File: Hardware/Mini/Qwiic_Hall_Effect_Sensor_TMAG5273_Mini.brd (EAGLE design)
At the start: 25.4 x 12.7 mm, 40 parts, among them J1 Vertical Qwiic Connector, J2 Vertical Qwiic Connector, Q1 20V/4.2A/52mΩ/1.4W, U1 TMAG5273

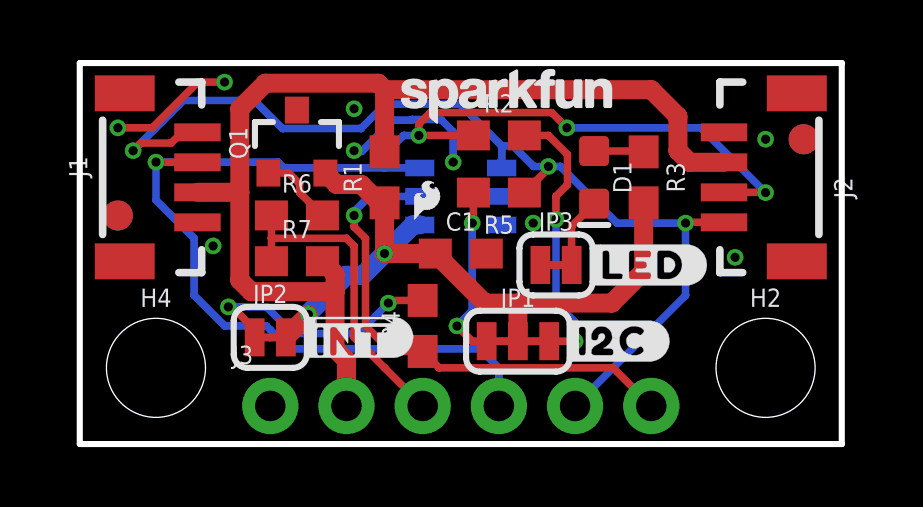
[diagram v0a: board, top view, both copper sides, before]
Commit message: Updates for design review
Changed LED and associated resistor to have the correct part and value; added dimension lines and further notes on the layout; adjusted aesthetics in schematic to now be the same as each other (minus the change in Qwiic connectors and number of standoffs)
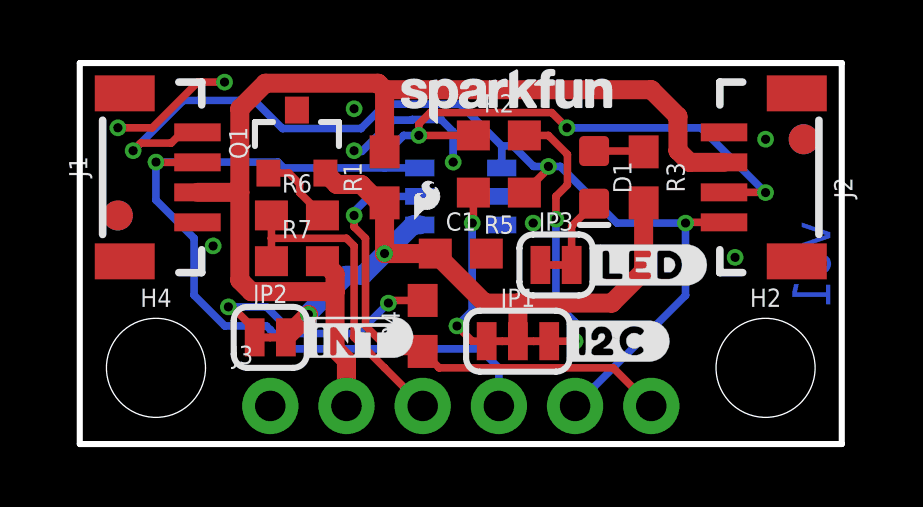
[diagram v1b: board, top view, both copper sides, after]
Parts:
- D1: value RED -> Red
- R3: value 1k -> 4.7k
- moved LOGO5 48.3 mm to (44.5, 50.8)
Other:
- board text added: "Solder Mask: Red Thickness: 1.6mm Two layer design Finish: HASL Lead-Free Copper Weight: 1oz Material: TG135-140"
- board text added: "v01"
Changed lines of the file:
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@@
 <layer number="45" name="Holes" color="7" fill="1" visible="yes" active="yes"/>
 <layer number="46" name="Milling" color="3" fill="1" visible="no" active="yes"/>
-<layer number="47" name="Measures" color="7" fill="1" visible="no" active="yes"/>
+<layer number="47" name="Measures" color="7" fill="1" visible="yes" active="yes"/>
 <layer number="48" name="Document" color="7" fill="1" visible="no" active="yes"/>
 <layer number="49" name="Reference" color="7" fill="1" visible="no" active="yes"/>
@@
 <wire x1="25.4" y1="12.7" x2="0" y2="12.7" width="0.2032" layer="20"/>
 <wire x1="0" y1="12.7" x2="0" y2="0" width="0.2032" layer="20"/>
+<text x="45.72" y="40.64" size="1.778" layer="51" font="vector" align="top-left">Solder Mask: Red
+Thickness: 1.6mm
+Two layer design
+Finish: HASL Lead-Free
+Copper Weight: 1oz
+Material: TG135-140</text>
+<dimension x1="5.08" y1="8.89" x2="5.08" y2="0" x3="-2.54" y3="4.445" textsize="1.778" layer="47" unit="inch"/>
+<dimension x1="0" y1="12.7" x2="0" y2="0" x3="-6.35" y3="6.35" textsize="1.778" layer="47" unit="inch"/>
+<dimension x1="19.05" y1="1.27" x2="19.05" y2="0" x3="29.21" y3="0.635" textsize="1.778" layer="47" unit="inch"/>
+<dimension x1="22.86" y1="2.54" x2="22.86" y2="0" x3="34.29" y3="1.27" textsize="1.778" layer="47" unit="inch"/>
+<dimension x1="22.86" y1="2.54" x2="0" y2="2.54" x3="11.43" y3="-3.81" textsize="1.778" layer="47" unit="inch"/>
+<dimension x1="25.4" y1="0" x2="0" y2="0" x3="12.7" y3="-7.62" textsize="1.778" layer="47" unit="inch"/>
+<dimension x1="6.35" y1="1.27" x2="0" y2="1.27" x3="3.175" y3="15.24" textsize="1.778" layer="47" unit="inch"/>
+<dimension x1="4.699" y1="8.89" x2="0" y2="8.89" x3="2.3495" y3="19.05" textsize="1.778" layer="47" unit="inch"/>
+<dimension x1="2.54" y1="2.54" x2="0" y2="2.54" x3="1.27" y3="22.86" textsize="1.778" layer="47" unit="inch"/>
+<text x="24.384" y="5.969" size="1.27" layer="16" font="vector" ratio="15" rot="SMR270" align="center">v01</text>
 </plain>
 <attributes>
@@
 </autorouter>
 <elements>
-<element name="D1" library="SparkFun-LED" package="LED-0603" value="RED" x="17.145" y="8.89" smashed="yes" rot="R270">
-<attribute name="NAME" x="17.78" y="8.89" size="0.6096" layer="25" font="vector" ratio="20" rot="R270" align="bottom-center"/>
-<attribute name="PROD_ID" value="DIO-00819" x="-53.975" y="-55.88" size="1.778" layer="27" rot="R270" display="off"/>
-<attribute name="VALUE" x="16.51" y="8.89" size="0.6096" layer="27" font="vector" ratio="20" rot="R270" align="top-center"/>
-</element>
 <element name="FD1" library="SparkFun-Aesthetics" package="FIDUCIAL-1X2" value="FIDUCIAL1X2" x="24.13" y="10.16" smashed="yes"/>
 <element name="FD2" library="SparkFun-Aesthetics" package="FIDUCIAL-1X2" value="FIDUCIAL1X2" x="1.27" y="7.62" smashed="yes"/>
@@
 <element name="LOGO3" library="SparkFun-Aesthetics" package="QWIIC_4MM" value="QWIIC_LOGO_4MM" x="22.86" y="7.366" smashed="yes" rot="MR0"/>
 <element name="LOGO4" library="SparkFun-Aesthetics" package="SFE_LOGO_NAME_7MM" value="SFE_LOGO_NAME7_MM" x="14.224" y="11.684" smashed="yes"/>
-<element name="LOGO5" library="SparkFun-Aesthetics" package="ORDERING_INSTRUCTIONS" value="SPECIAL_INSTRUCTIONS-ORDERING" x="92.71" y="50.8" smashed="yes"/>
+<element name="LOGO5" library="SparkFun-Aesthetics" package="ORDERING_INSTRUCTIONS" value="SPECIAL_INSTRUCTIONS-ORDERING" x="44.45" y="50.8" smashed="yes"/>
 <element name="LOGO6" library="SparkFun-Aesthetics" package="SFE_LOGO_FLAME_.05" value="SFE_LOGO_FLAME0.05_INCH" x="11.557" y="8.128" smashed="yes"/>
 <element name="R2" library="SparkFun-Resistors" package="0603" value="2.2k" x="13.97" y="10.287" smashed="yes">
@@
 <attribute name="PROD_ID" value="RES-08272" x="59.69" y="-60.833" size="1.778" layer="27" display="off"/>
 <attribute name="VALUE" x="13.97" y="9.525" size="0.6096" layer="27" font="vector" ratio="20" align="top-center"/>
-</element>
-<element name="R3" library="SparkFun-Resistors" package="0603" value="1k" x="18.796" y="8.89" smashed="yes" rot="R270">
-<attribute name="NAME" x="19.558" y="8.89" size="0.6096" layer="25" font="vector" ratio="20" rot="R270" align="bottom-center"/>
-<attribute name="PROD_ID" value="RES-07856" x="-52.324" y="-40.64" size="1.778" layer="27" rot="R270" display="off"/>
-<attribute name="VALUE" x="18.034" y="8.89" size="0.6096" layer="27" font="vector" ratio="20" rot="R270" align="top-center"/>
 </element>
 <element name="R4" library="SparkFun-Resistors" package="0603" value="10k" x="11.43" y="3.937" smashed="yes" rot="R90">
@@
 <element name="U$9" library="output" package="#RST#5279" value="" x="11.43" y="3.81" smashed="yes" rot="MR270"/>
 <element name="U$10" library="output" package="#LED#5275" value="" x="18.796" y="5.969" smashed="yes"/>
+<element name="D1" library="SparkFun-LED" package="LED-0603" value="Red" x="17.145" y="8.89" smashed="yes" rot="R270">
+<attribute name="NAME" x="17.78" y="8.89" size="0.6096" layer="25" font="vector" ratio="20" rot="R270" align="bottom-center"/>
+<attribute name="PROD_ID" value="DIO-17976" x="17.145" y="8.89" size="1.778" layer="27" font="vector" rot="R270" display="off"/>
+<attribute name="VALUE" x="16.51" y="8.89" size="0.6096" layer="27" font="vector" ratio="20" rot="R270" align="top-center"/>
+</element>
+<element name="R3" library="SparkFun-Resistors" package="0603" value="4.7k" x="18.796" y="8.89" smashed="yes" rot="R270">
+<attribute name="NAME" x="19.558" y="8.89" size="0.6096" layer="25" font="vector" ratio="20" rot="R270" align="bottom-center"/>
+<attribute name="PROD_ID" value="RES-07857" x="18.796" y="8.89" size="1.778" layer="27" font="vector" rot="R270" display="off"/>
+<attribute name="VALUE" x="18.034" y="8.89" size="0.6096" layer="27" font="vector" ratio="20" rot="R270" align="top-center"/>
+</element>
 </elements>
 <signals>
@@
 </signal>
 <signal name="N$4">
-<contactref element="R3" pad="1"/>
 <contactref element="D1" pad="A"/>
 <wire x1="17.145" y1="9.767" x2="18.769" y2="9.767" width="0.254" layer="1"/>
-<wire x1="18.769" y1="9.767" x2="18.796" y2="9.74" width="0.254" layer="1"/>
+<contactref element="R3" pad="1"/>
+<wire x1="17.145" y1="9.767" x2="18.796" y2="9.74" width="0" layer="19" extent="1-1"/>
 </signal>
 <signal name="N$1">
 <contactref element="JP3" pad="2"/>
+<wire x1="16.3957" y1="5.969" x2="16.3957" y2="7.2637" width="0.254" layer="1"/>
 <contactref element="D1" pad="C"/>
-<wire x1="17.145" y1="8.013" x2="16.3957" y2="7.2637" width="0.254" layer="1"/>
-<wire x1="16.3957" y1="7.2637" x2="16.3957" y2="5.969" width="0.254" layer="1"/>
+<wire x1="16.3957" y1="7.2637" x2="17.145" y2="8.013" width="0.254" layer="1"/>
 </signal>
 <signal name="N$5">
@@
 <signal name="3.3V_SW">
 <contactref element="JP1" pad="2"/>
-<contactref element="R3" pad="2"/>
 <contactref element="JP2" pad="2"/>
 <contactref element="C1" pad="1"/>
@@
 <wire x1="10.16" y1="8.04" x2="10.16" y2="6.35" width="0.635" layer="1"/>
 <wire x1="11.85" y1="6.35" x2="13.501" y2="4.699" width="0.635" layer="1"/>
-<wire x1="18.796" y1="5.75948125" x2="18.796" y2="8.04" width="0.635" layer="1"/>
-<wire x1="17.73551875" y1="4.699" x2="18.796" y2="5.75948125" width="0.635" layer="1"/>
+<wire x1="18.796" y1="5.75948125" x2="17.73551875" y2="4.699" width="0.635" layer="1"/>
 <wire x1="13.501" y1="4.699" x2="14.605" y2="4.699" width="0.635" layer="1"/>
 <wire x1="14.605" y1="4.699" x2="17.73551875" y2="4.699" width="0.635" layer="1"/>
@@
 <wire x1="8.89" y1="5.6261" x2="7.62" y2="4.3561" width="0.635" layer="16"/>
 <wire x1="7.62" y1="4.318" x2="7.62" y2="4.3561" width="0.635" layer="16"/>
+<contactref element="R3" pad="2"/>
+<wire x1="18.796" y1="8.04" x2="18.796" y2="5.75948125" width="0.635" layer="1"/>
 </signal>
 <signal name="GPIO">
@@
 </drawing>
 <compatibility>
+<note version="6.3" minversion="6.2.2" severity="warning">
+Since Version 6.2.2 text objects can contain more than one line,
+which will not be processed correctly with this version.
+</note>
 <note version="8.3" severity="warning">
 Since Version 8.3, EAGLE supports URNs for individual library

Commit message: Ready for review
Updates from ENG Checklist - Small tweaks added  - updated ordering of PTH headers for SDA and SCL, fixed final errors on design
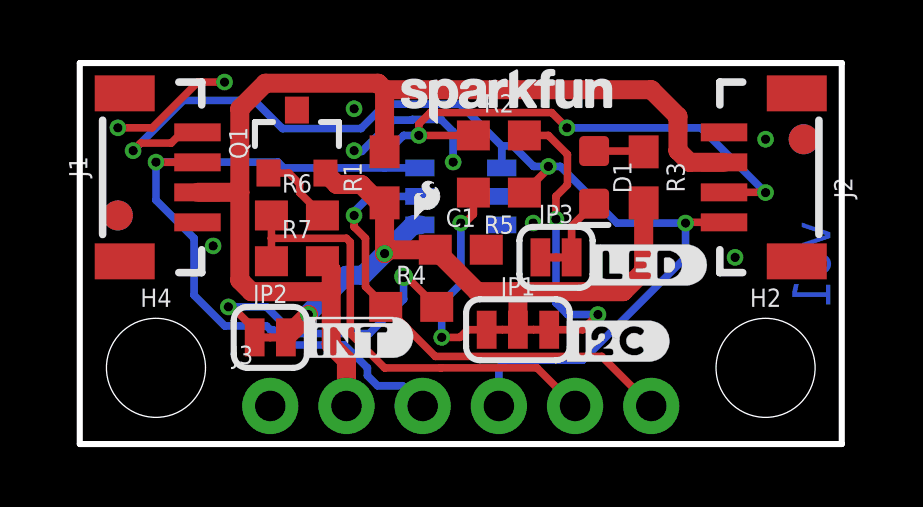
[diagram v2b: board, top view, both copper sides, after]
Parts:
- moved U$9 5.08 mm to (16.5, 3.81)
- moved U$2 2.54 mm to (14.0, 3.81)
- moved U$3 2.54 mm to (11.4, 3.94)
- moved R4 0.74 mm to (11.0, 4.57), turned to 0 degrees
- moved JP1 0.38 mm to (14.6, 3.81)
- moved JP3 0.25 mm to (15.9, 6.22)
- moved C1 0.13 mm to (12.7, 6.48)
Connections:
- net GPIO: now also J3.5; no longer J3.3
- net SCL: now also J3.4; no longer J3.5
- net SDA: now also J3.3; no longer J3.4
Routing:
- net GPIO: track 10.7 -> 15.7 mm
- net SDA: track 45.9 -> 42.8 mm
- net SCL: track 34.7 -> 37.3 mm
- net N$5: track 8.76 -> 10.4 mm
- net N$6: track 5.87 -> 6.94 mm
- net N$2: track 9.21 -> 10.2 mm
- net INT: track 17.0 -> 16.2 mm

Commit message: Updated !INT silk
Updated !INT silk  to be the correct end (now ( rather than < )
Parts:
- removed U$1: (no value), output:##INT#40
- added U$15: (no value), output:##INT#5276
- moved U$4 0.13 mm to (8.89, 3.94), turned to 270 degrees
- turned U$5 to 270 degrees
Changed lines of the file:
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@@
 <drawing>
 <settings>
-<setting alwaysvectorfont="no"/>
+<setting alwaysvectorfont="yes"/>
 <setting verticaltext="up"/>
 </settings>
@@
 <layer number="19" name="Unrouted" color="6" fill="1" visible="yes" active="yes"/>
 <layer number="20" name="Dimension" color="24" fill="1" visible="yes" active="yes"/>
-<layer number="21" name="tPlace" color="16" fill="1" visible="yes" active="yes"/>
+<layer number="21" name="tPlace" color="16" fill="1" visible="no" active="yes"/>
 <layer number="22" name="bPlace" color="14" fill="1" visible="yes" active="yes"/>
-<layer number="23" name="tOrigins" color="15" fill="1" visible="yes" active="yes"/>
+<layer number="23" name="tOrigins" color="15" fill="1" visible="no" active="yes"/>
 <layer number="24" name="bOrigins" color="15" fill="1" visible="yes" active="yes"/>
 <layer number="25" name="tNames" color="7" fill="1" visible="no" active="yes"/>
@@
 <layer number="37" name="tTest" color="7" fill="1" visible="no" active="yes"/>
 <layer number="38" name="bTest" color="7" fill="1" visible="no" active="yes"/>
-<layer number="39" name="tKeepout" color="4" fill="11" visible="yes" active="yes"/>
-<layer number="40" name="bKeepout" color="1" fill="11" visible="yes" active="yes"/>
-<layer number="41" name="tRestrict" color="4" fill="10" visible="yes" active="yes"/>
-<layer number="42" name="bRestrict" color="1" fill="10" visible="yes" active="yes"/>
+<layer number="39" name="tKeepout" color="4" fill="11" visible="no" active="yes"/>
+<layer number="40" name="bKeepout" color="1" fill="11" visible="no" active="yes"/>
+<layer number="41" name="tRestrict" color="4" fill="10" visible="no" active="yes"/>
+<layer number="42" name="bRestrict" color="1" fill="10" visible="no" active="yes"/>
 <layer number="43" name="vRestrict" color="2" fill="10" visible="no" active="yes"/>
 <layer number="44" name="Drills" color="7" fill="1" visible="no" active="yes"/>
@@
 <attribute name="VALUE" x="12.7" y="5.715" size="0.6096" layer="27" font="vector" ratio="20" align="top-center"/>
 </element>
-<element name="U$1" library="output" package="##INT#40" value="" x="19.05" y="3.683" smashed="yes" rot="MR270"/>
 <element name="U$2" library="output" package="#SCL#38" value="" x="13.97" y="3.81" smashed="yes" rot="MR270"/>
 <element name="U$3" library="output" package="#SDA#37" value="" x="11.43" y="3.937" smashed="yes" rot="MR270"/>
-<element name="U$4" library="output" package="#3V3#37" value="" x="8.89" y="3.81" smashed="yes" rot="MR90"/>
-<element name="U$5" library="output" package="#GND#36" value="" x="6.35" y="3.937" smashed="yes" rot="MR90"/>
+<element name="U$4" library="output" package="#3V3#37" value="" x="8.89" y="3.937" smashed="yes" rot="MR270"/>
+<element name="U$5" library="output" package="#GND#36" value="" x="6.35" y="3.937" smashed="yes" rot="MR270"/>
 <element name="U$6" library="output" package="TMAG5273_HALL#EFFECT_SENSOR0" value="" x="12.446" y="11.43" smashed="yes" rot="MR0"/>
 <element name="U$7" library="output" package="##INT#5275" value="" x="9.144" y="3.556" smashed="yes"/>
@@
 <attribute name="VALUE" x="18.034" y="8.89" size="0.6096" layer="27" font="vector" ratio="20" rot="R270" align="top-center"/>
 </element>
+<element name="U$15" library="output" package="##INT#5276" value="" x="19.05" y="3.683" smashed="yes" rot="MR270"/>
 </elements>
 <signals>

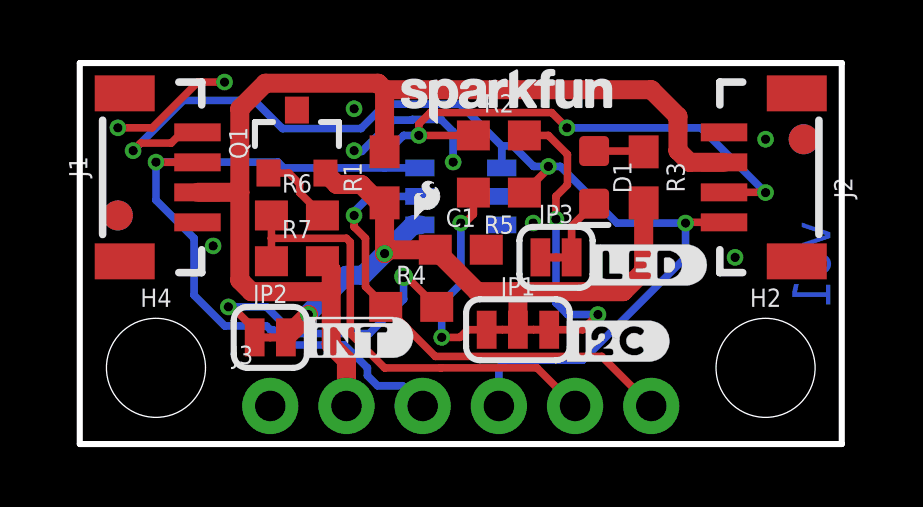
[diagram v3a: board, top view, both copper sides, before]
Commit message: Design Review Changes
Adjusted schematic to have the correct power-on reset circuit, along with the change in the layout. The GPIO net was relabled to RESET to match the layout of the board/labeling. Adjusted some labeling in the schematic.
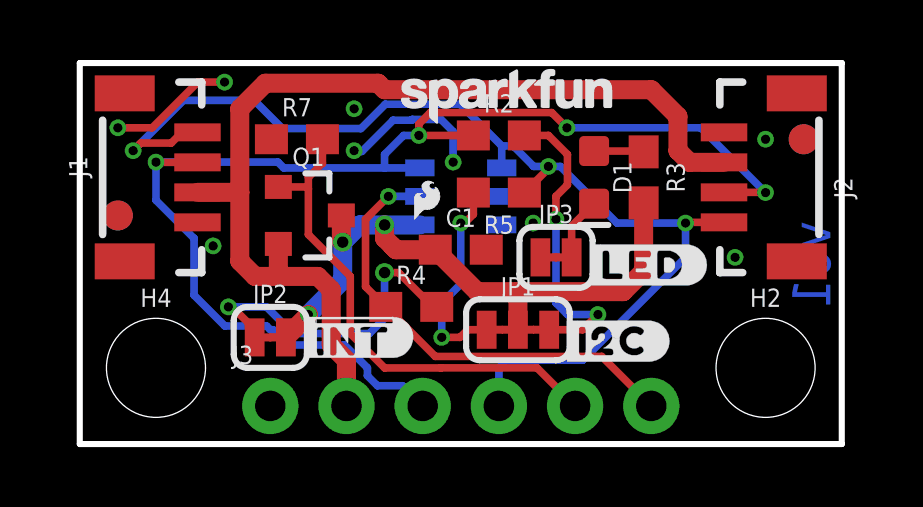
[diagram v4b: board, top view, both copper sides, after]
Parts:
- removed R1: 330, SparkFun-Resistors:0603
- removed R6: 10k, SparkFun-Resistors:0603
- moved R7 4.06 mm to (7.24, 10.2)
- moved Q1 2.44 mm to (7.62, 7.62), turned to 270 degrees
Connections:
- net INT renamed !INT
- removed net GPIO: J3.5, R6.1, R7.1
- removed net N$7: Q1.1, R6.2
- new net RESET: J3.5, Q1.1, R7.2
- net 3.3V: now also Q1.2; no longer R1.2, R7.2
- net 3.3V_SW: now also Q1.3; no longer Q1.2, R1.1
- net GND: now also R7.1; no longer Q1.3
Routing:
- net RESET: track 0.00 -> 16.8 mm
- net GPIO: track 15.7 -> 0.00 mm
- net N$7: track 2.56 -> 0.00 mm
- net 3.3V: track 35.8 -> 33.4 mm
- net 3.3V_SW: track 23.2 -> 21.3 mm, vias 2 -> 3
- net !INT: track 16.2 -> 15.5 mm
- net N$5: track 10.4 -> 11.0 mm

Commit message: Adjusted from design review
Added truth tables, changed RESET to Disable, adjusted magnetic axis to be centered to the middle of the board, added push button for 1x1 reset option
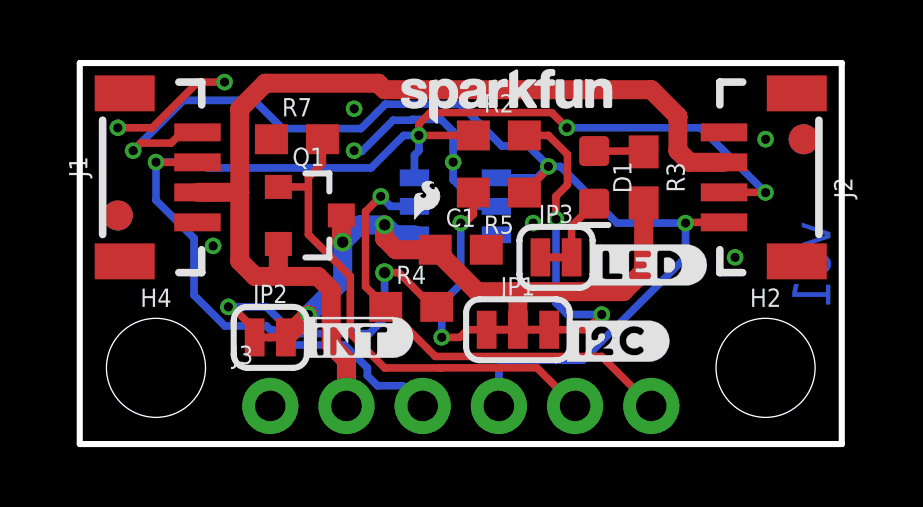
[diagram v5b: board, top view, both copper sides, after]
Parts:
- U$9: device output:#RST#5279 -> output:#DISABLE#5279
- moved U$9 1.65 mm to (16.5, 5.46)
- moved U1 0.38 mm to (12.5, 7.92)
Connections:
- net RESET renamed DISABLE
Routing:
- net GND: track 9.13 -> 11.5 mm
- net SCL: track 37.3 -> 38.4 mm
